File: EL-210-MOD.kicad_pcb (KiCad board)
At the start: 2 copper layers, 66 x 65 mm, 9 parts, among them P1 EL-210-KEY, U1 9-ST-20

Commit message: Rough layout of the digital part.
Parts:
- added U2: STM32G0B1KET6, Package_QFP:LQFP-32_7x7mm_P0.8mm, B.Cu at (146.9, 119.0)
- added U3: MAX6934AQH+D, Package_LCC:PLCC-44, B.Cu at (152.0, 100.5)
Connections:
- P1 pad 10: unconnected-(P1-Pad10) -> /KD3
- P1 pad 11: unconnected-(P1-Pad11) -> /KD2
- P1 pad 13: unconnected-(P1-Pad13) -> /KD1
- P1 pad 14: unconnected-(P1-Pad14) -> /KD0
- P1 pad 2: unconnected-(P1-Pad2) -> /KEY1
- P1 pad 3: unconnected-(P1-Pad3) -> /KEY2
- P1 pad 4: unconnected-(P1-Pad4) -> /KEY3
- P1 pad 5: unconnected-(P1-Pad5) -> /KD8
- P1 pad 6: unconnected-(P1-Pad6) -> /KD7
- P1 pad 7: unconnected-(P1-Pad7) -> /KD6
- P1 pad 8: unconnected-(P1-Pad8) -> /KD5
- P1 pad 9: unconnected-(P1-Pad9) -> /KD4
- U1 pad 1: unconnected-(U1-Pad1) -> /H1
- U1 pad 10: unconnected-(U1-Pad10) -> Net-(U1-Pad10)
- U1 pad 11: unconnected-(U1-Pad11) -> Net-(U1-Pad11)
- U1 pad 12: unconnected-(U1-Pad12) -> Net-(U1-Pad12)
- U1 pad 13: unconnected-(U1-Pad13) -> Net-(U1-Pad13)
- U1 pad 14: unconnected-(U1-Pad14) -> Net-(U1-Pad14)
- U1 pad 15: unconnected-(U1-Pad15) -> Net-(U1-Pad15)
- U1 pad 16: unconnected-(U1-Pad16) -> Net-(U1-Pad16)
- U1 pad 17: unconnected-(U1-Pad17) -> Net-(U1-Pad17)
- U1 pad 18: unconnected-(U1-Pad18) -> Net-(U1-Pad18)
- U1 pad 19: unconnected-(U1-Pad19) -> /H2
- U1 pad 2: unconnected-(U1-Pad2) -> /SEG_A
- U1 pad 3: unconnected-(U1-Pad3) -> Net-(U1-Pad3)
- U1 pad 4: unconnected-(U1-Pad4) -> Net-(U1-Pad4)
- U1 pad 5: unconnected-(U1-Pad5) -> Net-(U1-Pad5)
- U1 pad 6: unconnected-(U1-Pad6) -> Net-(U1-Pad6)
- U1 pad 7: unconnected-(U1-Pad7) -> Net-(U1-Pad7)
- U1 pad 8: unconnected-(U1-Pad8) -> Net-(U1-Pad8)
- U1 pad 9: unconnected-(U1-Pad9) -> Net-(U1-Pad9)
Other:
- board text removed: "3.3v"
- board text removed: "Akashi-10 v1.0.2"
- board text removed: "GND"
- board text removed: "https://github.com/suikan4github/Akashi-10"

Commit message: Schematics is finished.
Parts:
- added C1: 1u, Capacitor_SMD:C_0603_1608Metric_Pad1.08x0.95mm_HandSolder, F.Cu at (155.2, 78.3)
- added C10: C, Capacitor_SMD:C_0603_1608Metric_Pad1.08x0.95mm_HandSolder, F.Cu at (167.3, 62.1)
- added C11: UZG1H100MCL1GB, Capacitor_SMD:CP_Elec_4x3.9, F.Cu at (156.9, 59.0)
- added C2: C, Capacitor_SMD:C_0603_1608Metric_Pad1.08x0.95mm_HandSolder, F.Cu at (163.9, 67.2)
- added C3: C, Capacitor_SMD:C_0603_1608Metric_Pad1.08x0.95mm_HandSolder, F.Cu at (155.2, 73.3)
- added C4: 0.1u, Capacitor_SMD:C_0603_1608Metric_Pad1.08x0.95mm_HandSolder, F.Cu at (170.3, 57.3)
- added C5: 1u, Capacitor_SMD:C_0603_1608Metric_Pad1.08x0.95mm_HandSolder, F.Cu at (155.2, 70.8)
- added C6: UZG0J220MCL1GB, Capacitor_SMD:CP_Elec_6.3x3.9, F.Cu at (134.5, 74.9)
- added C7: C, Capacitor_SMD:C_0603_1608Metric_Pad1.08x0.95mm_HandSolder, F.Cu at (171.7, 59.8)
- added C8: C, Capacitor_SMD:C_0603_1608Metric_Pad1.08x0.95mm_HandSolder, F.Cu at (163.9, 64.7)
- added C9: 0.1u, Capacitor_SMD:C_0603_1608Metric_Pad1.08x0.95mm_HandSolder, F.Cu at (159.5, 65.8)
- added D1: D_Schottky, Diode_SMD:D_0603_1608Metric_Pad1.05x0.95mm_HandSolder, F.Cu at (163.0, 62.1)
- added D2: D_Schottky, Diode_SMD:D_0603_1608Metric_Pad1.05x0.95mm_HandSolder, F.Cu at (155.2, 63.2)
- added J1: Conn_01x05, Connector_PinHeader_2.54mm:PinHeader_1x05_P2.54mm_Horizontal, F.Cu at (131.6, 58.4)
- added L1: LQH5BPN4R7N38L, project_lib:LQH5BPN100M38L, F.Cu at (149.5, 76.5)
- added L2: LQH5BPN100M38L, project_lib:LQH5BPN100M38L, F.Cu at (149.5, 64.6)
- added R1: 330, Resistor_SMD:R_0603_1608Metric_Pad0.98x0.95mm_HandSolder, F.Cu at (159.5, 70.8)
- added R2: 18, Resistor_SMD:R_0603_1608Metric_Pad0.98x0.95mm_HandSolder, F.Cu at (155.2, 65.8)
- added R3: 18, Resistor_SMD:R_0603_1608Metric_Pad0.98x0.95mm_HandSolder, F.Cu at (155.2, 68.3)
- added R4: 61.9k, Resistor_SMD:R_0603_1608Metric_Pad0.98x0.95mm_HandSolder, F.Cu at (159.5, 68.3)
- added R5: 2.15k, Resistor_SMD:R_0603_1608Metric_Pad0.98x0.95mm_HandSolder, F.Cu at (155.2, 75.8)
- added U4: TPS613221ADBV, Package_TO_SOT_SMD:SOT-23-5, F.Cu at (109.0, 73.0)
- added U5: MAX4719EUB+, Package_SO:MSOP-10_3x3mm_P0.5mm, F.Cu at (164.4, 58.4)
- added U6: TLV61046ADB, Package_TO_SOT_SMD:SOT-23-6, F.Cu at (114.2, 73.0)
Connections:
- U2 pad 31: /LPUART2_RX -> /LPUART2_TX
- U3 pad 1: unconnected-(U3-Pad1) -> +24V
- U3 pad 18: unconnected-(U3-Pad18) -> -2V5
- U3 pad 44: unconnected-(U3-Pad44) -> +3V3

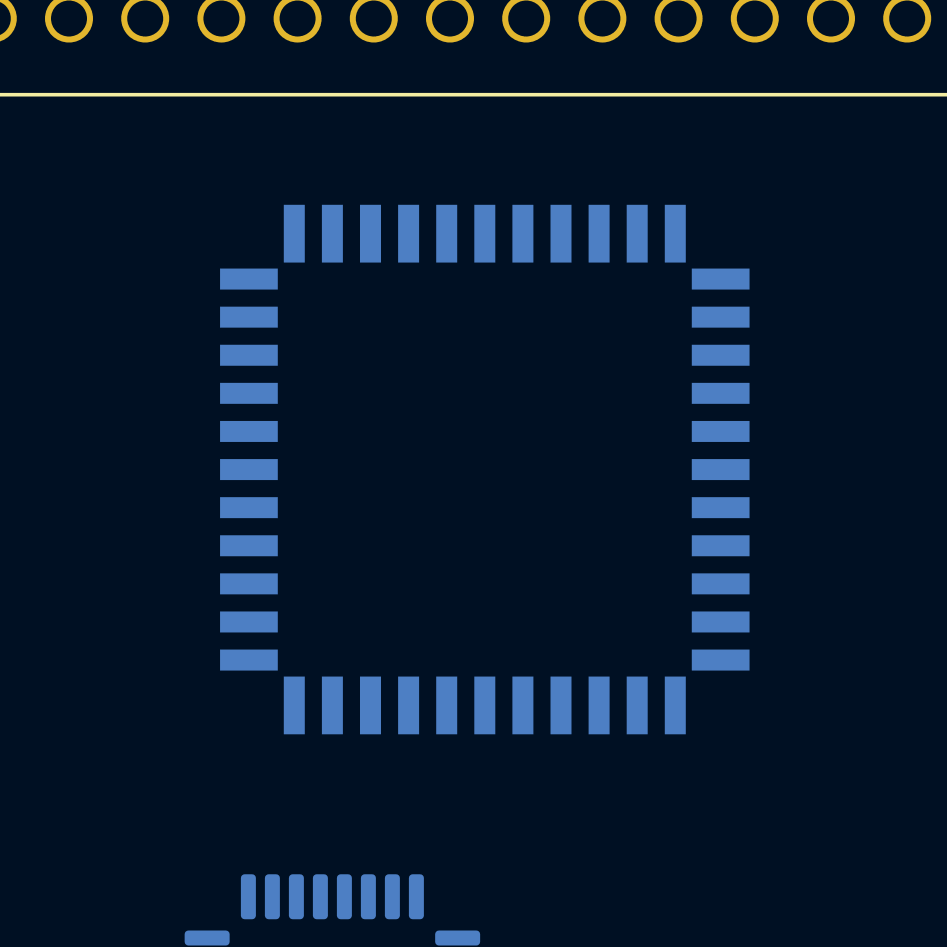
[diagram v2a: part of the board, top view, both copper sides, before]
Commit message: Change PLCC footprint to handsolder type
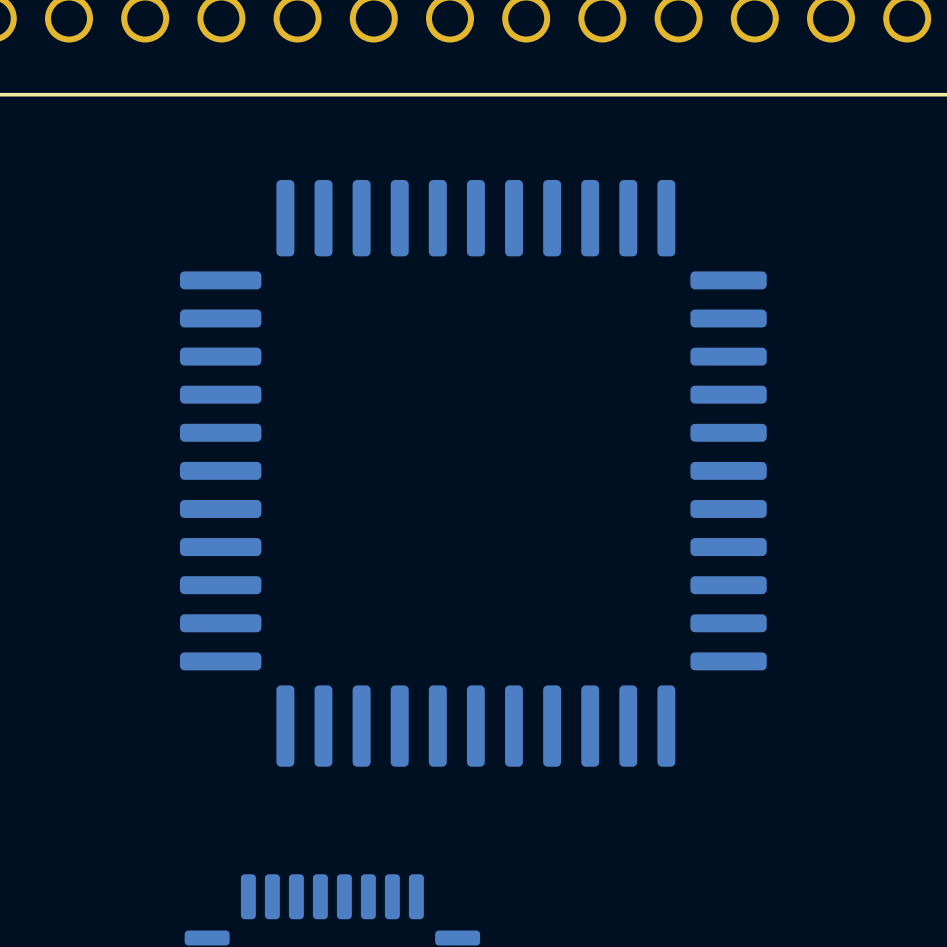
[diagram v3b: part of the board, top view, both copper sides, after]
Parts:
- U3: footprint Package_LCC:PLCC-44 -> plcc44_hs:PLCC44_handsoldering

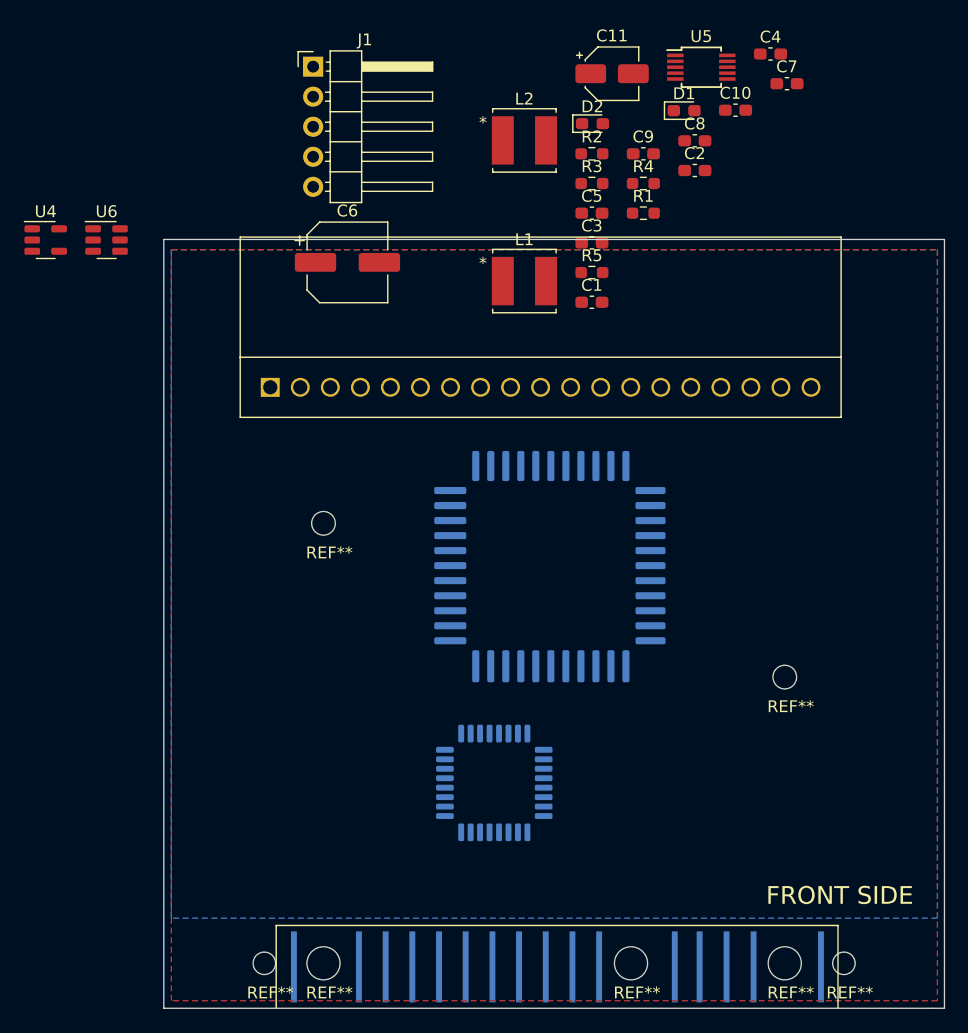
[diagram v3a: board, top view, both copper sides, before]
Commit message: parts placed.
The version number is written.
The SMD pad of the Ls are modifed.
Routing is not finished.
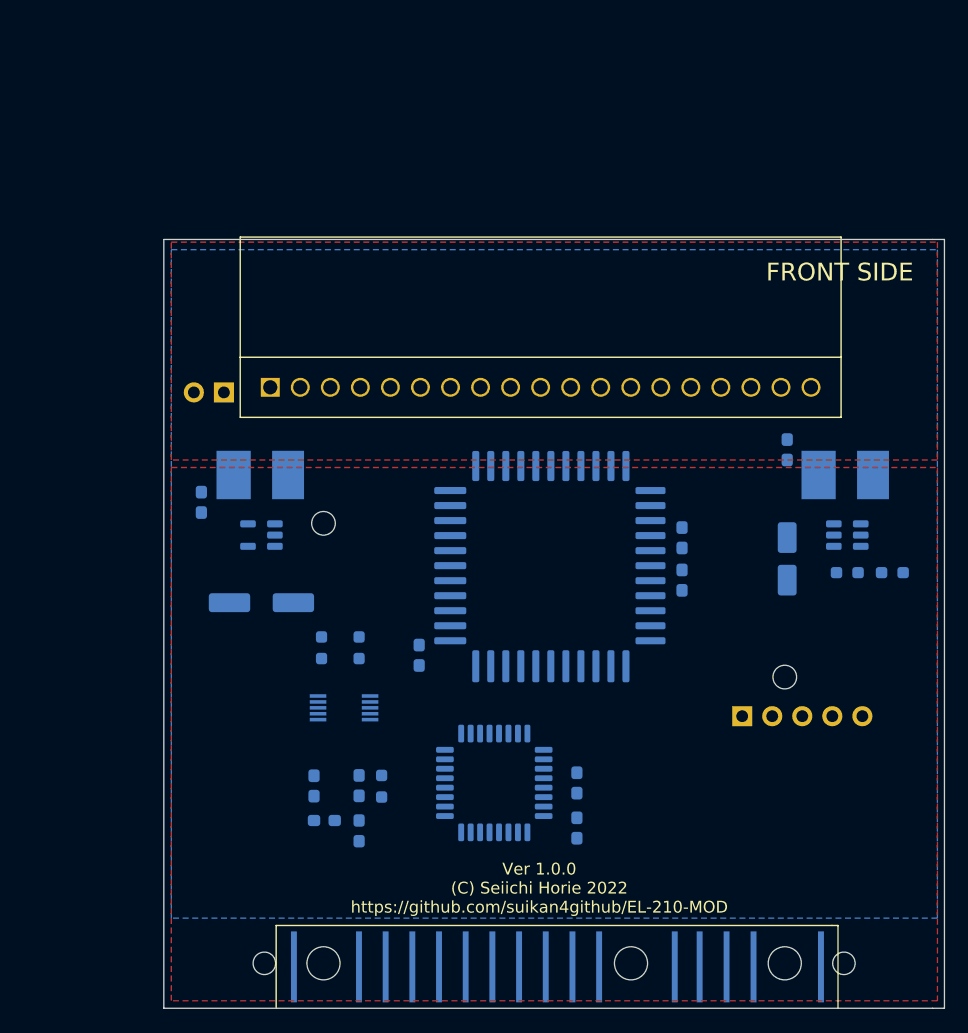
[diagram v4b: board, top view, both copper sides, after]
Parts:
- added J2: Conn_01x02, Connector_PinHeader_2.54mm:PinHeader_1x02_P2.54mm_Vertical, B.Cu at (124.1, 85.9)
- C1, C11, C4, C5, C6, C9, D1, D2, J1, L1, L2, R1, R2, R3, R4, R5, U4, U5, U6: moved to B.Cu
- C10, C2, C3, C7, C8: value C -> 0.1u; moved to B.Cu
- moved U6 67.4 mm to (176.8, 98.0), turned to 180 degrees
- moved D1 66.8 mm to (135.5, 123.0), turned to 90 degrees
- moved J1 65.8 mm to (167.9, 113.3), turned to -90 degrees
- moved D2 63.1 mm to (132.6, 122.1), turned to 180 degrees
- moved U5 62.0 mm to (134.2, 112.6), turned to 180 degrees
- moved C4 61.3 mm to (122.2, 95.2), turned to -90 degrees
- moved C7 57.5 mm to (140.6, 108.2), turned to -90 degrees
- moved C2 56.5 mm to (153.9, 122.8), turned to -90 degrees
- moved C5 53.8 mm to (131.7, 119.2), turned to 90 degrees
- moved R1 53.3 mm to (137.4, 119.2), turned to 90 degrees
- moved R2 46.2 mm to (135.5, 107.5), turned to -90 degrees
- moved C3 45.7 mm to (153.9, 119.0), turned to 90 degrees
- moved R3 45.4 mm to (132.3, 107.5), turned to 90 degrees
- moved C1 45.4 mm to (135.5, 119.2), turned to -90 degrees
- moved C11 43.6 mm to (171.7, 100.0), turned to -90 degrees
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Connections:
- U2 pad 19: /TIM2_CH2 -> /TIM2_CH1
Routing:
- added copper zone on F.Cu, net +3V3
- added copper zone on F.Cu, net +BATT
- removed copper zone on F.Cu, net (none)
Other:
- board text added: "+BATT"
- board text added: "EL-210-MOD"
- board text added: "GND"
- board text added: "NRST"
- board text added: "SWCLK"
- board text added: "SWDIO"
- board text added: "TXD"
- board text added: "Ver 1.0.0 (C) Seiichi Horie 2022 https://github.com/suikan4github/EL-210-MOD"

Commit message: Layout refined.
Higher parts are moved to the front side to avoid the
touch with the back cabinet.
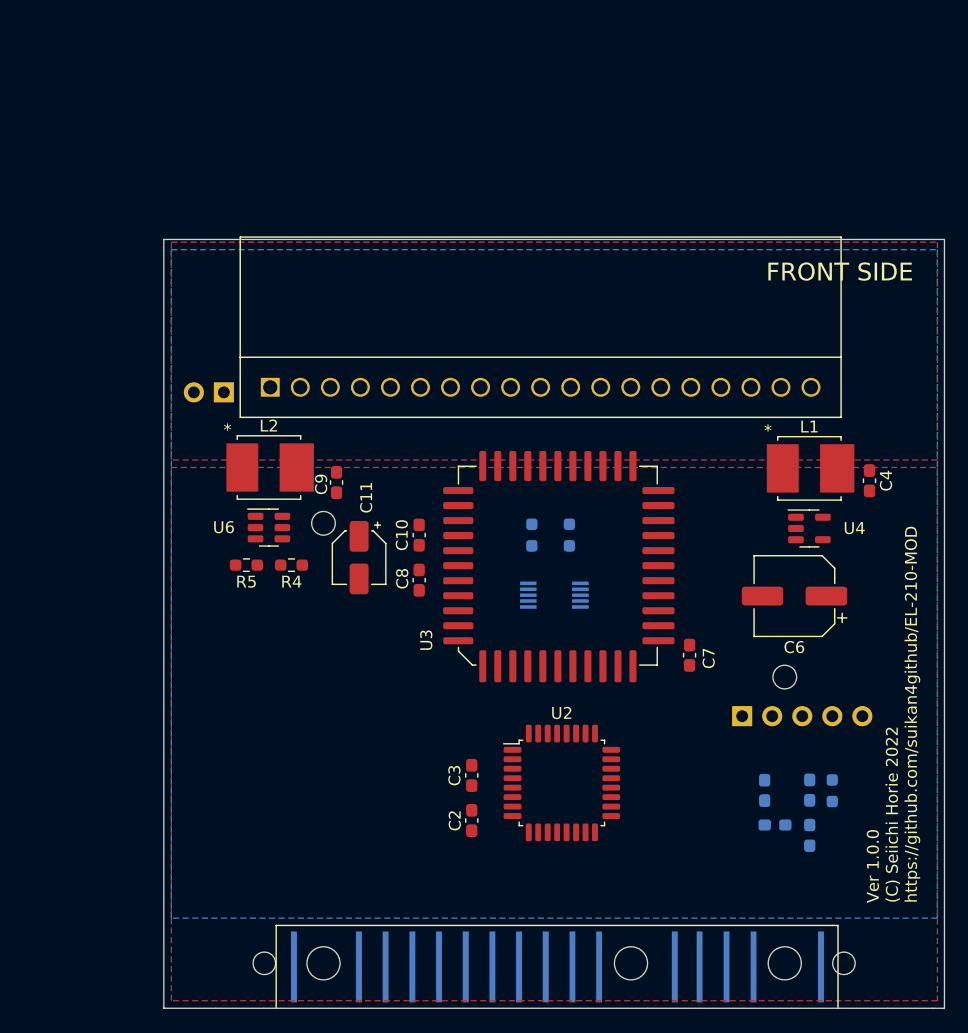
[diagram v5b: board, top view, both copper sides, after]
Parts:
- C10, C11, C2, C3, C4, C6, C7, C8, C9, L1, L2, R4, R5, U2, U3, U4, U6: moved to F.Cu
- moved C4 56.5 mm to (178.7, 93.4)
- moved R5 54.6 mm to (126.0, 100.5), turned to 180 degrees
- moved U6 48.9 mm to (127.9, 97.4), turned to 0 degrees
- moved L2 48.8 mm to (127.9, 92.3), turned to 0 degrees
- moved R4 47.0 mm to (129.8, 100.5), turned to 180 degrees
- moved L1 46.3 mm to (173.6, 92.4), turned to 0 degrees
- moved U4 46.3 mm to (173.6, 97.4), turned to 0 degrees
- moved C6 45.1 mm to (172.3, 103.2), turned to 180 degrees
- moved C9 38.2 mm to (133.6, 93.5), turned to -90 degrees
- moved C1 38.1 mm to (173.6, 119.6)
- moved C5 38.1 mm to (169.8, 119.6)
- moved D1 38.1 mm to (173.6, 123.4)
- moved D2 38.1 mm to (170.7, 122.5)
- moved R1 38.1 mm to (175.5, 119.6)
- moved C11 36.2 mm to (135.5, 99.9)
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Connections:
- U1 pad 10: Net-(U1-Pad10) -> Net-(U3-Pad35)
- U1 pad 11: Net-(U1-Pad11) -> Net-(U3-Pad34)
- U1 pad 12: Net-(U1-Pad12) -> Net-(U3-Pad33)
- U1 pad 13: Net-(U1-Pad13) -> Net-(U3-Pad32)
- U1 pad 14: Net-(U1-Pad14) -> Net-(U3-Pad31)
- U1 pad 15: Net-(U1-Pad15) -> Net-(U3-Pad30)
- U1 pad 16: Net-(U1-Pad16) -> Net-(U3-Pad27)
- U1 pad 17: Net-(U1-Pad17) -> Net-(U3-Pad26)
- U1 pad 18: Net-(U1-Pad18) -> Net-(U3-Pad25)
- U1 pad 3: Net-(U1-Pad3) -> Net-(U3-Pad42)
- U1 pad 4: Net-(U1-Pad4) -> Net-(U3-Pad41)
- U1 pad 5: Net-(U1-Pad5) -> Net-(U3-Pad40)
- U1 pad 6: Net-(U1-Pad6) -> Net-(U3-Pad39)
- U1 pad 7: Net-(U1-Pad7) -> Net-(U3-Pad38)
- U1 pad 8: Net-(U1-Pad8) -> Net-(U3-Pad37)
- U1 pad 9: Net-(U1-Pad9) -> Net-(U3-Pad36)
- U2 pad 10: /KD3 -> /KD8
- U2 pad 11: /KD4 -> /KD7
- U2 pad 12: /KD5 -> /KD6
- U2 pad 13: /KD6 -> /KD5
- U2 pad 15: /KD7 -> /KD4
- U2 pad 16: /KD8 -> /KD3
- U2 pad 17: /KEY3 -> /KD2
- U2 pad 20: /KEY2 -> /KD1
- U2 pad 21: /KEY1 -> /KD0
- U2 pad 7: /KD0 -> /KEY1
- U2 pad 8: /KD1 -> /KEY2
- U2 pad 9: /KD2 -> /KEY3
- U3 pad 25: Net-(U1-Pad3) -> Net-(U3-Pad25)
- U3 pad 26: Net-(U1-Pad4) -> Net-(U3-Pad26)
- U3 pad 27: Net-(U1-Pad5) -> Net-(U3-Pad27)
- U3 pad 30: Net-(U1-Pad6) -> Net-(U3-Pad30)
- U3 pad 31: Net-(U1-Pad7) -> Net-(U3-Pad31)
- U3 pad 32: Net-(U1-Pad8) -> Net-(U3-Pad32)
- U3 pad 33: Net-(U1-Pad9) -> Net-(U3-Pad33)
- U3 pad 34: Net-(U1-Pad10) -> Net-(U3-Pad34)
- U3 pad 35: Net-(U1-Pad11) -> Net-(U3-Pad35)
- U3 pad 36: Net-(U1-Pad12) -> Net-(U3-Pad36)
- U3 pad 37: Net-(U1-Pad13) -> Net-(U3-Pad37)
- U3 pad 38: Net-(U1-Pad14) -> Net-(U3-Pad38)
- U3 pad 39: Net-(U1-Pad15) -> Net-(U3-Pad39)
- U3 pad 40: Net-(U1-Pad16) -> Net-(U3-Pad40)
- U3 pad 41: Net-(U1-Pad17) -> Net-(U3-Pad41)
- U3 pad 42: Net-(U1-Pad18) -> Net-(U3-Pad42)

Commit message: Layout finished.
DRC passed except silkscreen minor problem.
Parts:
- C1, C5, D1, D2, R1: moved to F.Cu
- turned D2 to 0 degrees
- renumbered REF** to H1, REF** to H2, REF** to H3, REF** to H4, REF** to H5, REF** to H6, REF** to H7
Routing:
- net GND: track 0.00 -> 53.2 mm, vias 0 -> 17
- net /SEG_A: track 0.00 -> 38.5 mm
- net /NRST: track 0.00 -> 34.0 mm, vias 0 -> 1
- net /LPUART2_TX: track 0.00 -> 32.5 mm, vias 0 -> 1
- net /LOAD: track 0.00 -> 31.4 mm, vias 0 -> 2
- net /EN24V: track 0.00 -> 28.8 mm
- net -2V5: track 0.00 -> 28.0 mm
- net /H1: track 0.00 -> 27.3 mm, vias 0 -> 2
- net /H2: track 0.00 -> 25.4 mm, vias 0 -> 2
- net +3V3: track 0.00 -> 24.5 mm, vias 0 -> 8
- net /TIM2_CH1: track 0.00 -> 24.5 mm
- net /TIM1_CH1: track 0.00 -> 23.7 mm, vias 0 -> 1
- net /SPI1_MOSI: track 0.00 -> 21.8 mm
- net /KEY1: track 0.00 -> 21.4 mm, vias 0 -> 1
- net /TIM1_CH1N: track 0.00 -> 21.3 mm, vias 0 -> 1
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
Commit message: Gerber file generated
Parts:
- C11: value UZG1H100MCL1GB -> 10u
- C6: value UZG0J220MCL1GB -> 22u
- L1: value LQH5BPN4R7N38L -> 4.7uH
- L2: value LQH5BPN100M38L -> 10uH
- moved J1 10.2 mm to (178.1, 113.2), turned to 90 degrees
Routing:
- net /SWCLK: track 13.1 -> 24.3 mm, vias 0 -> 1
- net /LPUART2_TX: track 32.5 -> 23.3 mm
- net /NRST: track 34.0 -> 31.4 mm
- net GND: track 53.2 -> 51.3 mm
- net -2V5: track 28.0 -> 29.2 mm

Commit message: Corrected signal name from TIM2_CH1 to TIM1_CH2
Fixed typo. Layout is not changed.
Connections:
- net /TIM2_CH1 renamed /TIM1_CH2
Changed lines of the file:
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@@
   (net 78 "Net-(C1-Pad1)")
   (net 79 "Net-(C1-Pad2)")
-  (net 80 "/TIM2_CH1")
+  (net 80 "/TIM1_CH2")
   (net 81 "Net-(R2-Pad2)")
   (net 82 "Net-(R3-Pad1)")
@@
     (fp_line (start 0.8 0.4125) (end -0.8 0.4125) (layer "F.Fab") (width 0.1))
     (pad "1" smd roundrect (at -0.9125 0 90) (size 0.975 0.95) (layers "F.Cu" "F.Paste" "F.Mask") (roundrect_rratio 0.25)
-      (net 80 "/TIM2_CH1") (pintype "passive"))
+      (net 80 "/TIM1_CH2") (pintype "passive"))
     (pad "2" smd roundrect (at 0.9125 0 90) (size 0.975 0.95) (layers "F.Cu" "F.Paste" "F.Mask") (roundrect_rratio 0.25)
       (net 78 "Net-(C1-Pad1)") (pintype "passive"))
@@
       (net 54 "/TIM1_CH1") (pinfunction "PA8") (pintype "bidirectional"))
     (pad "19" smd roundrect (at 4.175 1.2) (size 1.5 0.5) (layers "F.Cu" "F.Paste" "F.Mask") (roundrect_rratio 0.25)
-      (net 80 "/TIM2_CH1") (pinfunction "PA9") (pintype "bidirectional"))
+      (net 80 "/TIM1_CH2") (pinfunction "PA9") (pintype "bidirectional"))
     (pad "20" smd roundrect (at 4.175 0.4) (size 1.5 0.5) (layers "F.Cu" "F.Paste" "F.Mask") (roundrect_rratio 0.25)
       (net 72 "/KD1") (pinfunction "PC6") (pintype "bidirectional"))
